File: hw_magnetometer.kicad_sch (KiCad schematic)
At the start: 4 parts

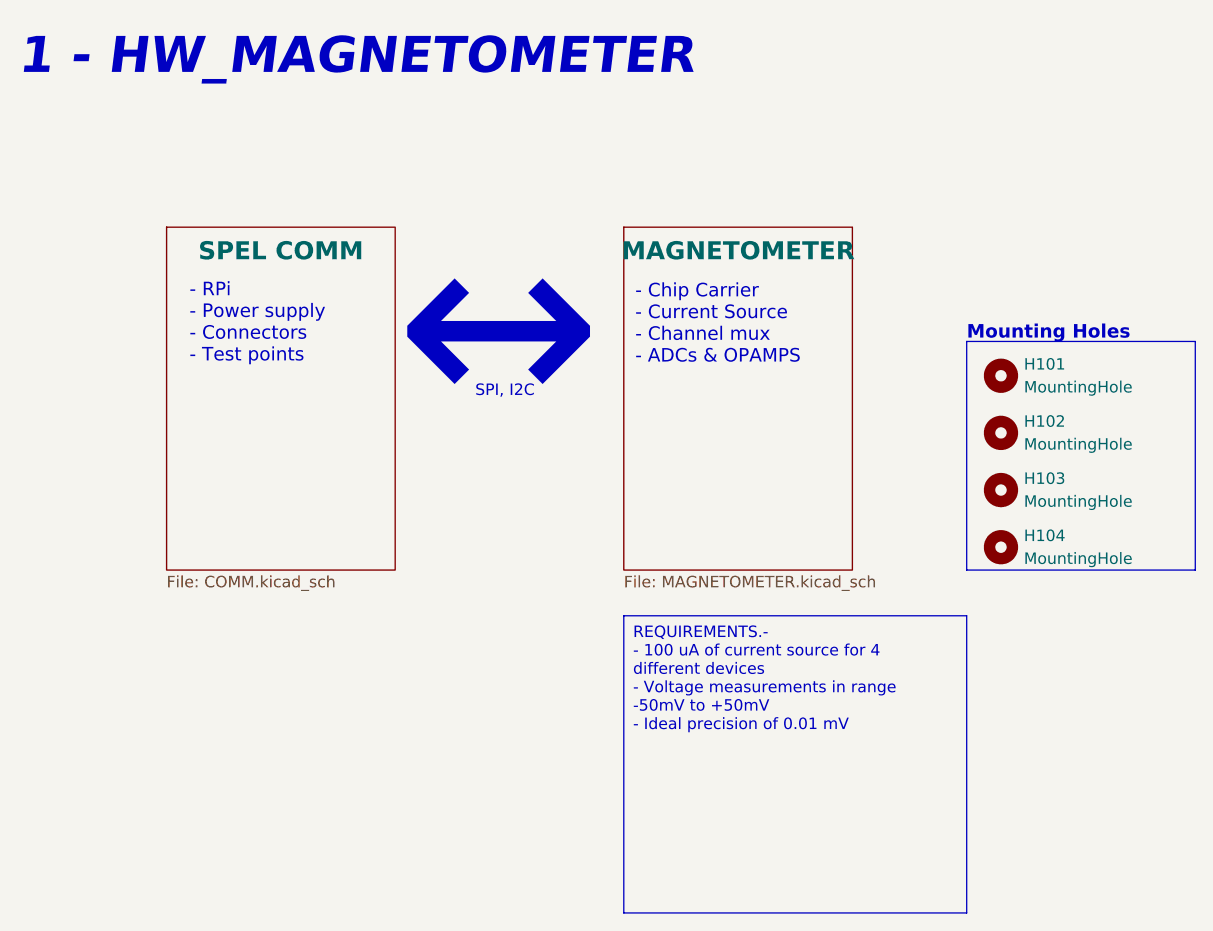
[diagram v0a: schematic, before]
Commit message: updated root page, sym and fp libs
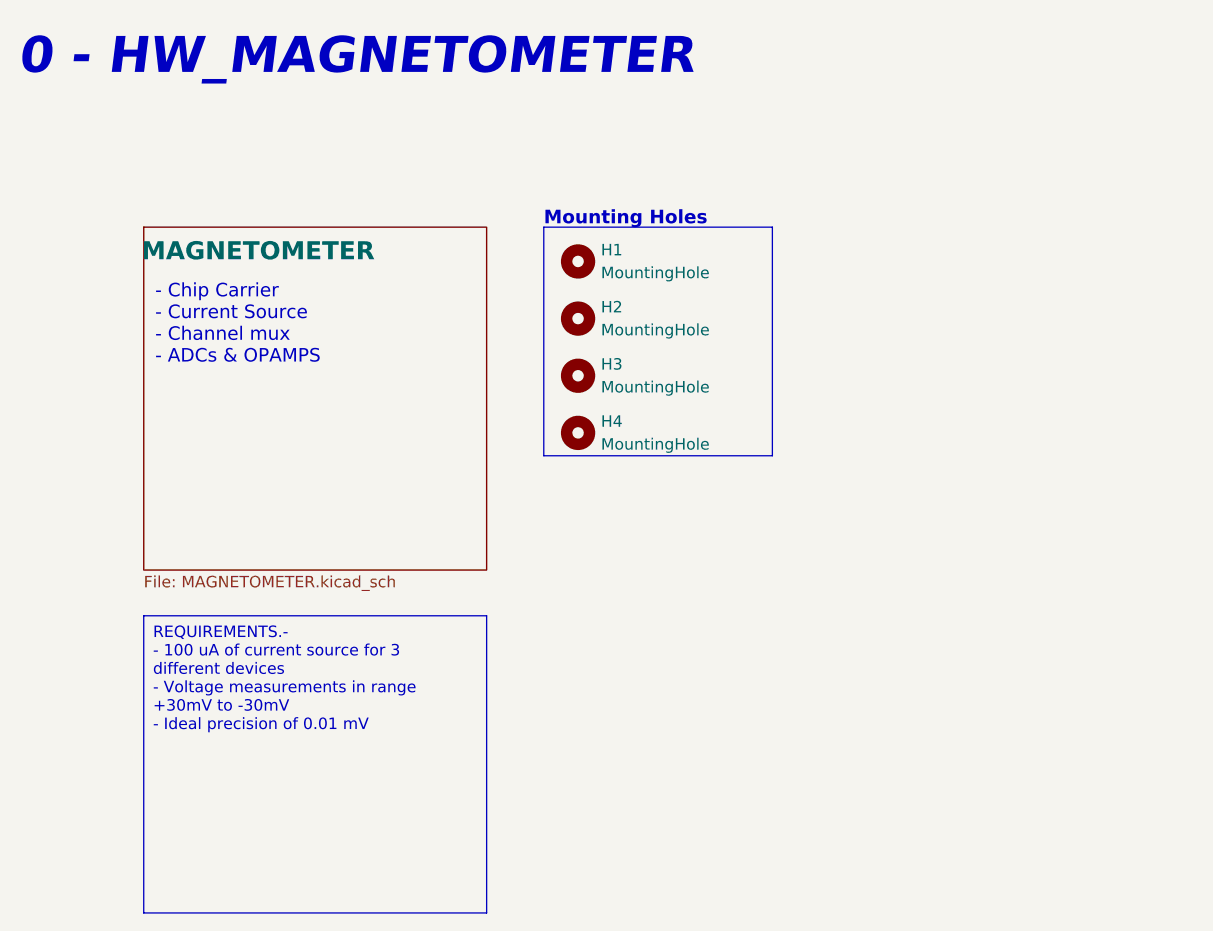
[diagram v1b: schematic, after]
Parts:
- renumbered H101 to H1, H102 to H2, H103 to H3, H104 to H4
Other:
- removed sheet SPEL COMM
- note added: "0 - HW_MAGNETOMETER"
- note removed: "- RPi - Power supply - Connectors - Test points"
- note removed: "1 - HW_MAGNETOMETER"
- note removed: "SPI, I2C"
- note removed: "↔"
- moved on the sheet: H1, H2, H3, H4
